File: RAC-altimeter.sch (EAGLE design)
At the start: 37 parts, among them J1 282834-2, J2 CORTEX_DEBUG_SMD, J3 MICRO-SD, J4 JUMPER-SMT_2_NO_SILK, U1 MAX32660GTP+, U2 BMI088, U3 BMP388, U4 RN4871-I_RM130, U5 MCP1640T-I_CHY, Y1 32.768kHz

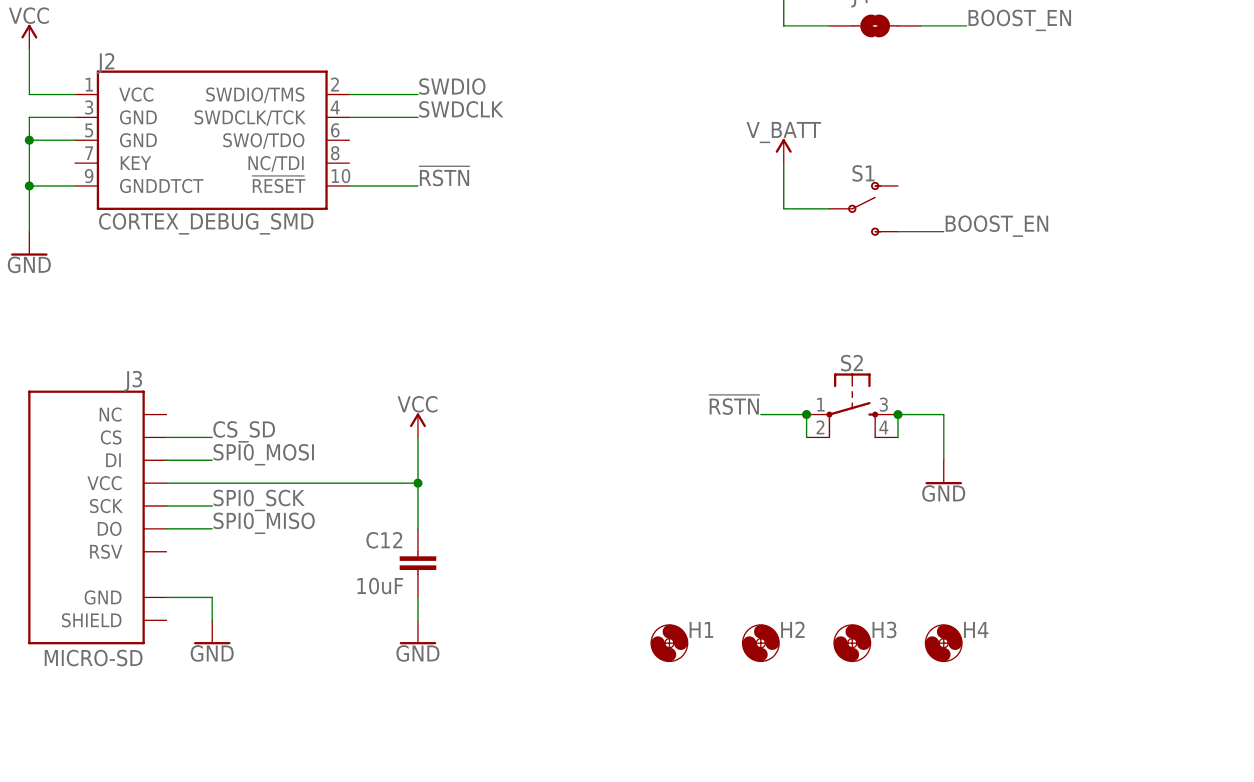
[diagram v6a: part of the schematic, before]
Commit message: Closed loose nets and finished routing
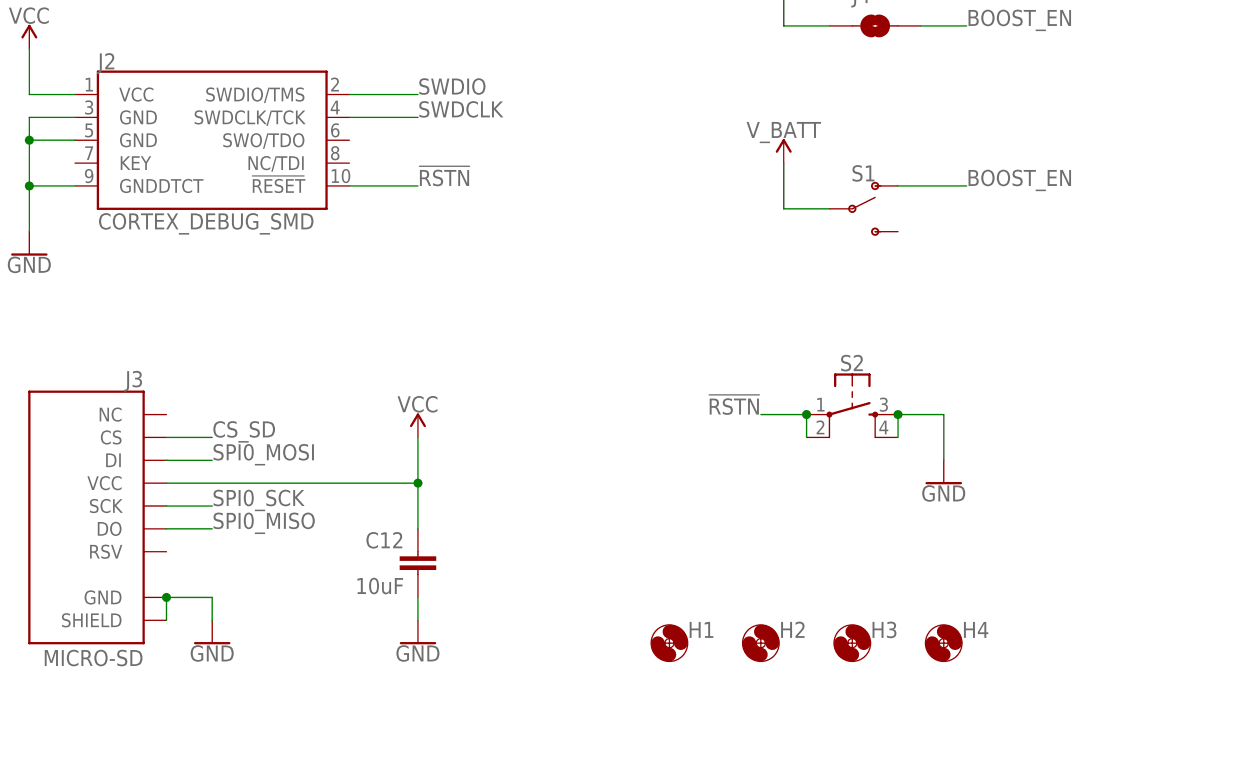
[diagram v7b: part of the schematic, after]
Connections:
- net BOOST_EN: now also S1.O; no longer S1.S
- net GND: now also J3.SHIELD
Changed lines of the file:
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@@
 <pinref part="GND1" gate="1" pin="GND"/>
 <wire x1="-157.48" y1="38.1" x2="-157.48" y2="35.56" width="0.1524" layer="91"/>
+<pinref part="J3" gate="J1" pin="SHIELD"/>
+<wire x1="-162.56" y1="35.56" x2="-162.56" y2="38.1" width="0.1524" layer="91"/>
+<junction x="-162.56" y="38.1"/>
 </segment>
 <segment>
@@
 </segment>
 <segment>
-<pinref part="S1" gate="1" pin="S"/>
-<wire x1="-81.28" y1="78.74" x2="-76.2" y2="78.74" width="0.1524" layer="91"/>
-<label x="-76.2" y="78.74" size="1.778" layer="95"/>
-</segment>
-<segment>
 <pinref part="J4" gate="G$1" pin="2"/>
 <wire x1="-78.74" y1="101.6" x2="-73.66" y2="101.6" width="0.1524" layer="91"/>
 <label x="-73.66" y="101.6" size="1.778" layer="95"/>
 </segment>
-</net>
+<segment>
+<pinref part="S1" gate="1" pin="O"/>
+<wire x1="-81.28" y1="83.82" x2="-73.66" y2="83.82" width="0.1524" layer="91"/>
+<label x="-73.66" y="83.82" size="1.778" layer="95"/>
+</segment>
+</net>

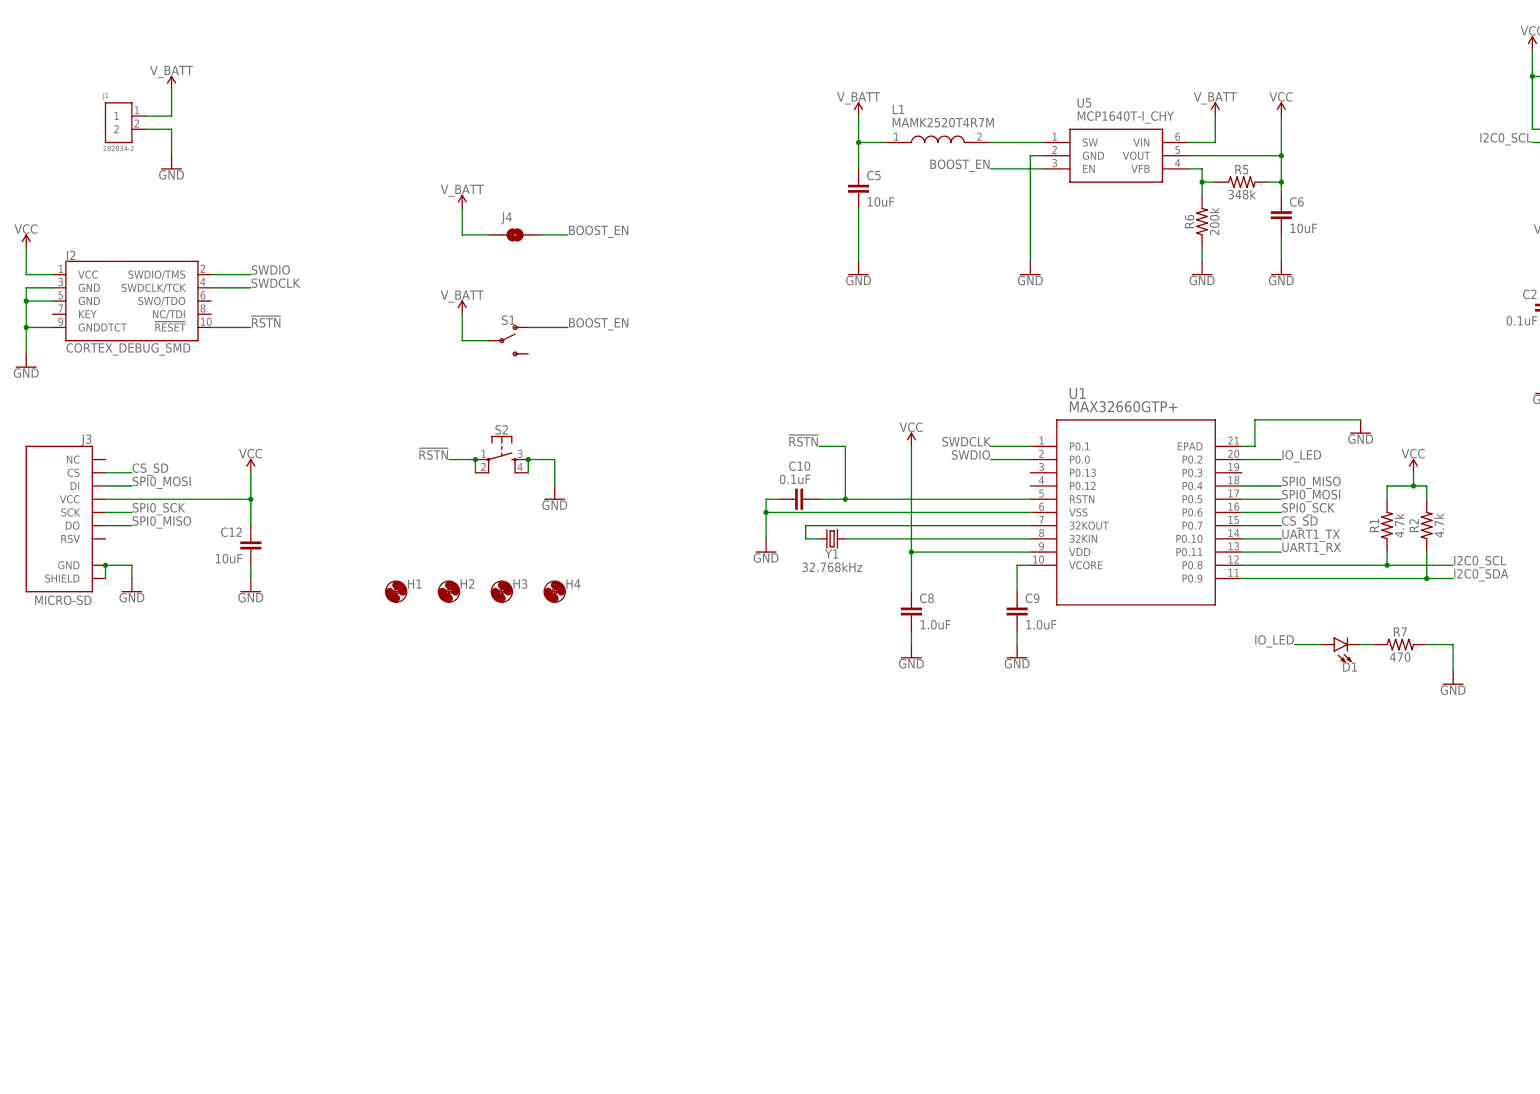
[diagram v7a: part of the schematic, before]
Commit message: Replaced the SD card socket with a NAND flash IC
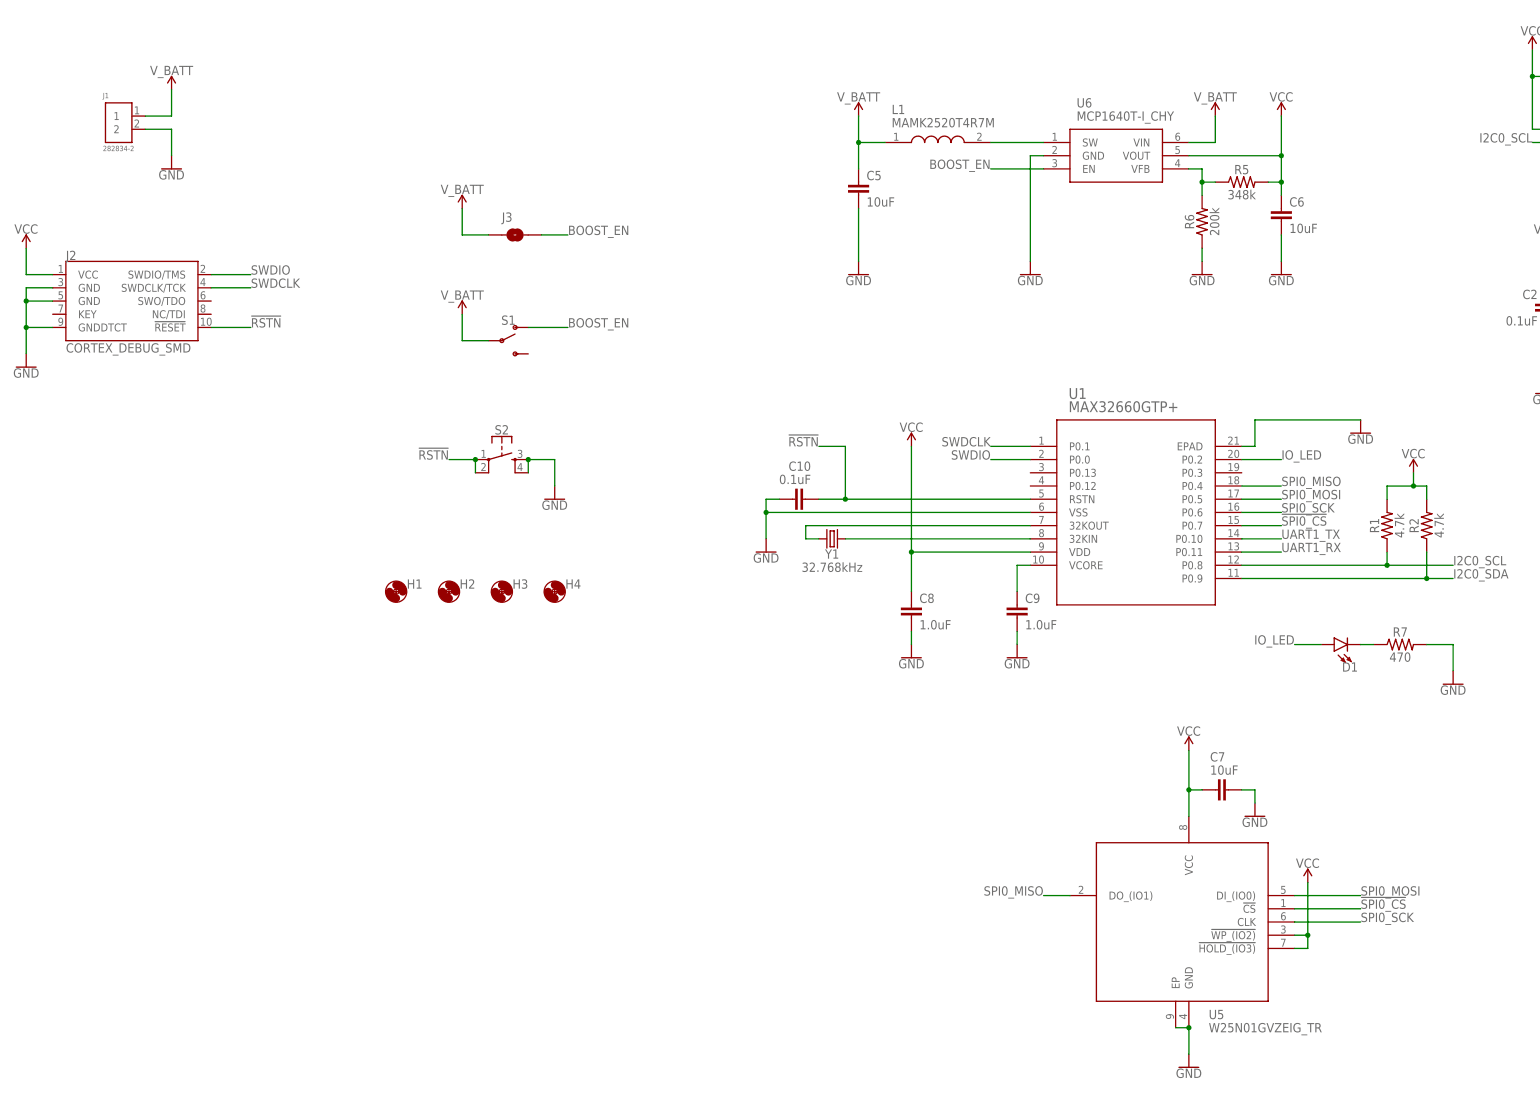
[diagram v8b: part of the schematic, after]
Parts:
- removed C12: 10uF, SparkFun-Capacitors:10UF-0603-6.3V-20%
- removed J4: JUMPER-SMT_2_NO_SILK, SparkFun-Jumpers:JUMPER-SMT_2_NO_SILK
- added C7: 10uF, SparkFun-Capacitors:10UF-0603-6.3V-20%
- added U6: MCP1640T-I_CHY, RAC-Altimeter:MCP1640T-I_CHY
- J3: value MICRO-SD -> JUMPER-SMT_2_NO_SILK; device SparkFun-Connectors:MICRO-SD_CARD_SOCKETTINY -> SparkFun-Jumpers:JUMPER-SMT_2_NO_SILK
- U5: value MCP1640T-I_CHY -> W25N01GVZEIG_TR; device RAC-Altimeter:MCP1640T-I_CHY -> RAC-Altimeter:W25N01GVZEIG_TR
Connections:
- removed net CS_SD: J3.CS, U1.P0.7
- new net !SPI0_CS: U1.P0.7, U5.!CS
- net BOOST_EN: now also J3.2, U6.EN; no longer J4.2, U5.EN
- net GND: now also C7.2, U5.EP, U6.GND; no longer C12.2, J3.GND, J3.SHIELD
- net SPI0_MISO: now also U5.DO_(IO1); no longer J3.DO
- net SPI0_MOSI: now also U5.DI_(IO0); no longer J3.DI
- net SPI0_SCK: now also U5.CLK; no longer J3.SCK
- net SW: now also U6.SW; no longer U5.SW
- net VCC: now also C7.1, U5.!HOLD_(IO3), U5.!WP_(IO2), U5.VCC, U6.VOUT; no longer C12.1, J3.VCC, U5.VOUT
- net VFB: now also U6.VFB; no longer U5.VFB
- net V_BATT: now also J3.1, U6.VIN; no longer J4.1, U5.VIN
